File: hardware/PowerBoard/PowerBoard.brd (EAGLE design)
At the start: 90 x 56 mm, 136 parts, among them J1 CON-HRS-DM3AT, J2 CON-ZX62R-B-5P, J3 CON-FTSH-105-01-L-DV-K, J4 CON-S2B-PH-SM4-TB, J5 CON-PJ-102A, J6 CON-71741-0002-TOP, J7 SWITCH-CJS-1200-1200, M1 MOUNT-HOLE3.3, M2 MOUNT-HOLE3.3, M3 MOUNT-HOLE3.3, M4 MOUNT-HOLE3.3, M5 FIDUCIAL1X2, M6 FIDUCIAL1X2, M7 FIDUCIAL1X2, M8 FIDUCIAL1X2, Q1 SI2323CDS, Q2 SI2312CDS, Q3 SI2333CDS, Q4 SI2333CDS, SW1 SWITCH-SPST, SW2 SWITCH-MS12ASG30, SW3 SWITCH-ESWITCH-TL3340G, U1 LTC4361-2DC, U10 MAX9938FEUK, U11 MAX9938FEUK, U12 MAX9938FEUK, U13 STM32F10XCXT6, U14 LTC2942-1, U15 USBLC6-2, U2 LTC4085, U3 XC6220B331MR-G, U4 XC6220B331MR-G, U5 XC9236A15DMR-G, U6 MIC94043, U8 MAX9938FEUK, U9 MAX9938FEUK, X1 ECX-2236, X2 ECX-31B

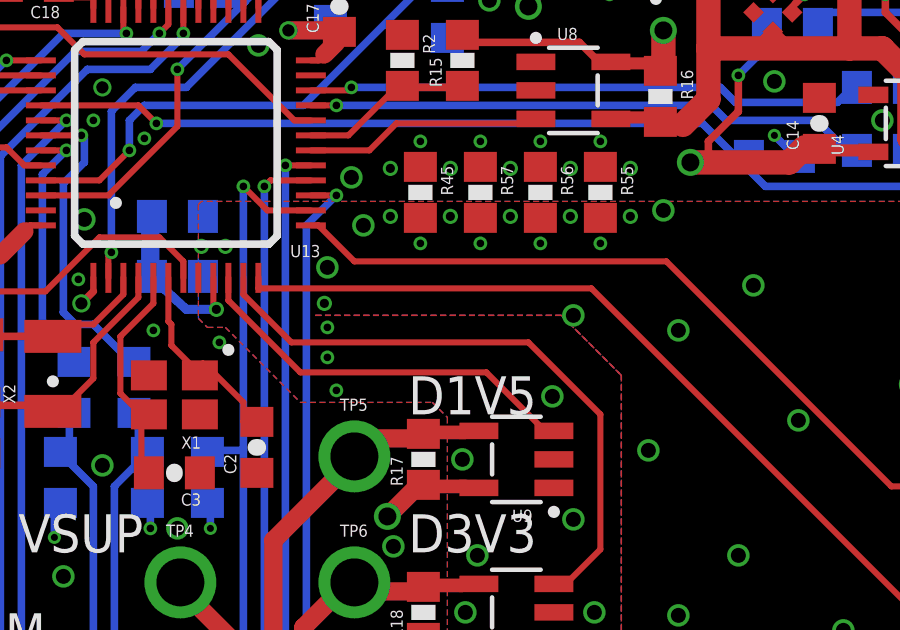
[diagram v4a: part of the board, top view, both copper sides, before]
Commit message: Modified ground plane cut-in.
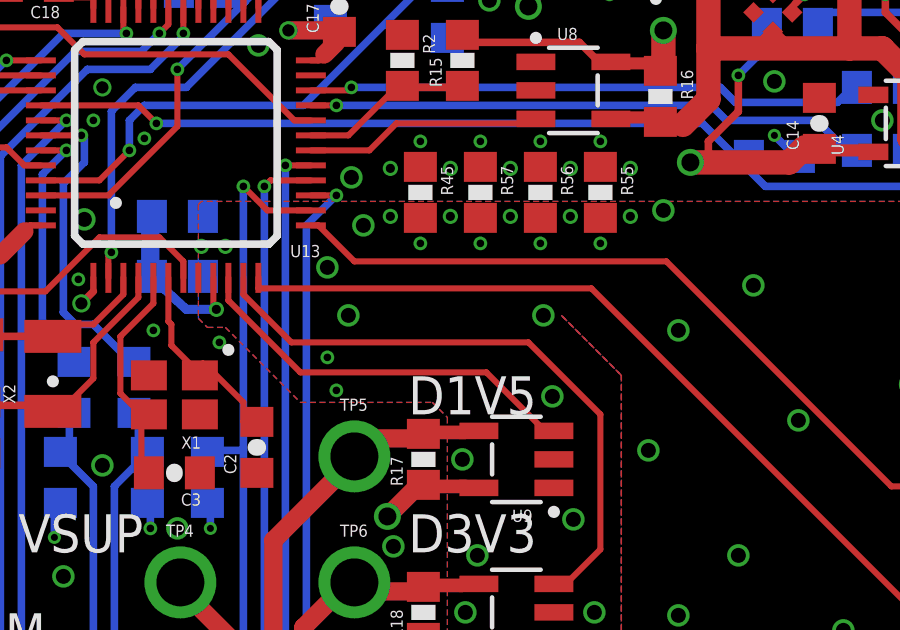
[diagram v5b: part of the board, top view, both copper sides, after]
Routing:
- net AGND: vias 87 -> 86
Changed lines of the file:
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@@
 <grid distance="0.5" unitdist="mm" unit="mm" style="lines" multiple="1" display="yes" altdistance="0.1" altunitdist="mm" altunit="mm"/>
 <layers>
-<layer number="1" name="Top" color="4" fill="1" visible="no" active="yes"/>
+<layer number="1" name="Top" color="4" fill="1" visible="yes" active="yes"/>
 <layer number="2" name="GND" color="2" fill="1" visible="no" active="yes"/>
 <layer number="3" name="SUPPLY" color="14" fill="1" visible="no" active="yes"/>
@@
 <layer number="15" name="Route15" color="4" fill="6" visible="no" active="no"/>
 <layer number="16" name="Bottom" color="11" fill="1" visible="no" active="yes"/>
-<layer number="17" name="Pads" color="2" fill="1" visible="no" active="yes"/>
-<layer number="18" name="Vias" color="2" fill="1" visible="no" active="yes"/>
+<layer number="17" name="Pads" color="2" fill="1" visible="yes" active="yes"/>
+<layer number="18" name="Vias" color="2" fill="1" visible="yes" active="yes"/>
 <layer number="19" name="Unrouted" color="6" fill="1" visible="yes" active="yes"/>
 <layer number="20" name="Dimension" color="15" fill="1" visible="yes" active="yes"/>
-<layer number="21" name="tPlace" color="7" fill="1" visible="no" active="yes"/>
+<layer number="21" name="tPlace" color="7" fill="1" visible="yes" active="yes"/>
 <layer number="22" name="bPlace" color="7" fill="1" visible="no" active="yes"/>
-<layer number="23" name="tOrigins" color="15" fill="1" visible="no" active="yes"/>
+<layer number="23" name="tOrigins" color="15" fill="1" visible="yes" active="yes"/>
 <layer number="24" name="bOrigins" color="15" fill="1" visible="no" active="yes"/>
 <layer number="25" name="tNames" color="7" fill="1" visible="no" active="yes"/>
@@
 <layer number="27" name="tValues" color="7" fill="1" visible="no" active="yes"/>
 <layer number="28" name="bValues" color="7" fill="1" visible="no" active="yes"/>
-<layer number="29" name="tStop" color="7" fill="3" visible="no" active="yes"/>
+<layer number="29" name="tStop" color="7" fill="3" visible="yes" active="yes"/>
 <layer number="30" name="bStop" color="7" fill="6" visible="no" active="yes"/>
 <layer number="31" name="tCream" color="7" fill="4" visible="no" active="yes"/>
@@
 <layer number="37" name="tTest" color="7" fill="1" visible="no" active="yes"/>
 <layer number="38" name="bTest" color="7" fill="1" visible="no" active="yes"/>
-<layer number="39" name="tKeepout" color="4" fill="11" visible="no" active="yes"/>
+<layer number="39" name="tKeepout" color="4" fill="11" visible="yes" active="yes"/>
 <layer number="40" name="bKeepout" color="1" fill="11" visible="no" active="yes"/>
 <layer number="41" name="tRestrict" color="4" fill="10" visible="no" active="yes"/>
@@
 <layer number="49" name="Reference" color="7" fill="1" visible="no" active="yes"/>
 <layer number="50" name="dxf" color="7" fill="1" visible="no" active="yes"/>
-<layer number="51" name="tDocu" color="14" fill="1" visible="no" active="yes"/>
+<layer number="51" name="tDocu" color="14" fill="1" visible="yes" active="yes"/>
 <layer number="52" name="bDocu" color="9" fill="1" visible="no" active="yes"/>
 <layer number="53" name="tGND_GNDA" color="7" fill="9" visible="no" active="no"/>
@@
 <via x="50.5" y="25" extent="1-16" drill="0.5"/>
 <via x="59.5" y="26" extent="1-16" drill="0.5"/>
-<via x="36.5" y="23" extent="1-16" drill="0.5"/>
+<via x="35.5" y="23" extent="1-16" drill="0.5"/>
 <via x="39" y="18.5" extent="1-16" drill="0.5"/>
 <via x="29.5" y="26" extent="1-16" drill="0.5"/>
@@
 <via x="42.5" y="24" extent="1-16" drill="0.5"/>
 <via x="28.3" y="24.6" extent="1-16" drill="0.5"/>
-<via x="28.2" y="23.4" extent="1-16" drill="0.3048"/>
 <via x="24.9" y="25.3" extent="1-16" drill="0.3048"/>
 <via x="24.1" y="25.3" extent="1-16" drill="0.3048"/>
@@
 <contactref element="U9" pad="1"/>
 <contactref element="U9" pad="2"/>
-<via x="28.3" y="22.6" extent="1-16" drill="0.254"/>
 <via x="28.3" y="21.6" extent="1-16" drill="0.254"/>
 <via x="28.6" y="20.5" extent="1-16" drill="0.254"/>
@@
 <via x="72.5" y="3.5" extent="1-16" drill="0.5"/>
 <via x="80" y="5" extent="1-16" drill="0.5"/>
+<via x="29" y="23" extent="1-16" drill="0.5"/>
 </signal>
 <signal name="VSUP">
@@
 <vertex x="38.1" y="21"/>
 <vertex x="36.1" y="23"/>
-<vertex x="27.9" y="23"/>
 <vertex x="36.1" y="23"/>
 <vertex x="38.1" y="21"/>
@@
 <vertex x="38.1" y="21"/>
 <vertex x="36.1" y="23"/>
-<vertex x="27.9" y="23"/>
 <vertex x="36.1" y="23"/>
 <vertex x="38.1" y="21"/>
@@
 <vertex x="38.1" y="21"/>
 <vertex x="36.1" y="23"/>
-<vertex x="27.9" y="23"/>
 <vertex x="36.1" y="23"/>
 <vertex x="38.1" y="21"/>
@@
 </signal>
 </signals>
-<errors>
-</errors>
 </board>
 </drawing>

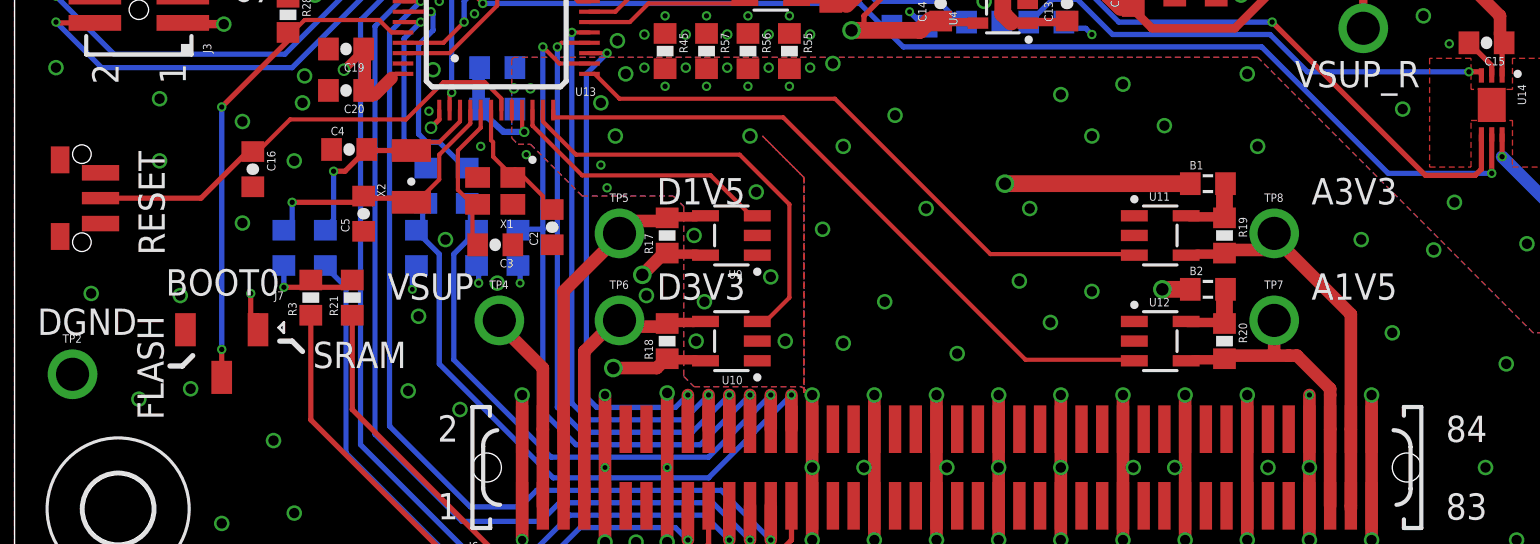
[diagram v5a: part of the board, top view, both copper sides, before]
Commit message: Adjusted BOOT switch and silk screen label positions.
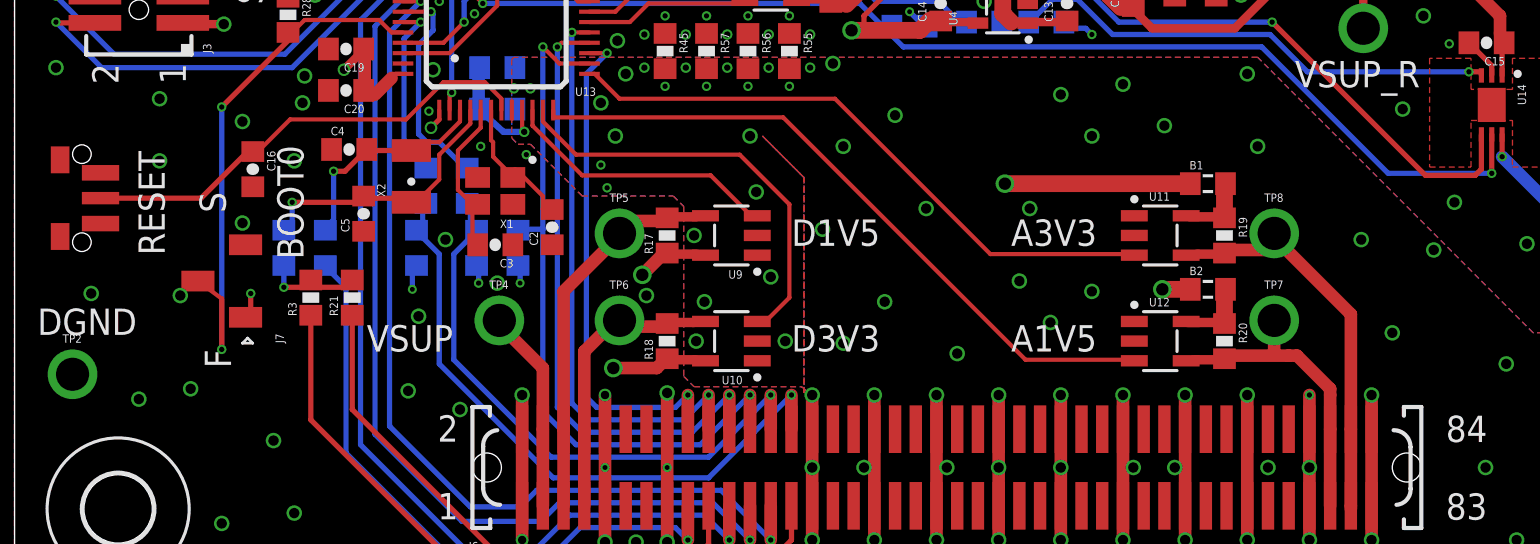
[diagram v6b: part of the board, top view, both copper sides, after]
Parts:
- moved J7 3.50 mm to (10.0, 16.0), turned to 90 degrees
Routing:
- net BOOT0: track 24.4 -> 26.9 mm
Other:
- board text added: "F"
- board text added: "S"
- board text removed: "FLASH"
- board text removed: "SRAM"
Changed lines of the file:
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@@
 <setting verticaltext="up"/>
 </settings>
-<grid distance="0.5" unitdist="mm" unit="mm" style="lines" multiple="1" display="yes" altdistance="0.1" altunitdist="mm" altunit="mm"/>
+<grid distance="1" unitdist="mm" unit="mm" style="lines" multiple="1" display="yes" altdistance="0.25" altunitdist="mm" altunit="mm"/>
 <layers>
 <layer number="1" name="Top" color="4" fill="1" visible="yes" active="yes"/>
@@
 <text x="60.75" y="54" size="1.27" layer="21" font="vector" rot="R180">OFF</text>
 <text x="80" y="54" size="1.27" layer="21" font="vector" rot="R180">ON</text>
-<text x="7.3" y="15.3" size="1.27" layer="21" font="vector">BOOT0</text>
+<text x="13.95" y="17.05" size="1.27" layer="21" font="vector" rot="R90">BOOT0</text>
 <text x="7.25" y="17.25" size="1.27" layer="21" font="vector" rot="R90">RESET</text>
 <text x="12" y="29.35" size="1.27" layer="21" font="vector" rot="R90">SWD</text>
@@
 <text x="85.25" y="37.25" size="1.27" layer="22" font="vector" rot="MR0">PWR SW</text>
 <text x="82.25" y="23.25" size="1.27" layer="22" font="vector" rot="MR0">BAT</text>
-<text x="14.4" y="11.8" size="1.27" layer="21" font="vector">SRAM</text>
-<text x="7.2" y="9.3" size="1.27" layer="21" font="vector" rot="R90">FLASH</text>
 <text x="82.15" y="13.4" size="1.27" layer="21" font="vector">AGND</text>
 <text x="1.1" y="13.4" size="1.27" layer="21" font="vector">DGND</text>
 <text x="67.25" y="35.75" size="1.27" layer="21" font="vector">VBAT</text>
-<text x="18" y="15.1" size="1.27" layer="21" font="vector">VSUP</text>
-<text x="31" y="15.1" size="1.27" layer="21" font="vector">D3V3</text>
-<text x="31" y="19.7" size="1.27" layer="21" font="vector">D1V5</text>
-<text x="62.6" y="15.1" size="1.27" layer="21" font="vector">A1V5</text>
-<text x="62.6" y="19.7" size="1.27" layer="21" font="vector">A3V3</text>
+<text x="17" y="12.6" size="1.27" layer="21" font="vector">VSUP</text>
+<text x="37.5" y="12.6" size="1.27" layer="21" font="vector">D3V3</text>
+<text x="37.5" y="17.7" size="1.27" layer="21" font="vector">D1V5</text>
+<text x="48.1" y="12.6" size="1.27" layer="21" font="vector">A1V5</text>
+<text x="48.1" y="17.7" size="1.27" layer="21" font="vector">A3V3</text>
 <text x="10.65" y="35.5" size="1.27" layer="21" font="vector">D3V3_STM</text>
 <text x="88" y="50" size="1.27" layer="21" font="vector" rot="R90">DGND</text>
@@
 <text x="70.75" y="2.75" size="1.27" layer="22" font="vector" rot="MR0">Vanderbilt University, ISIS</text>
 <circle x="54.5" y="5.2" radius="0.85" width="0.127" layer="22"/>
-<wire x1="13.9" y1="12.6" x2="13.4" y2="13.1" width="0.254" layer="21"/>
-<wire x1="13.4" y1="13.1" x2="12.8" y2="13.1" width="0.254" layer="21"/>
-<wire x1="8.6" y1="12.4" x2="8.1" y2="11.9" width="0.254" layer="21"/>
-<wire x1="8.1" y1="11.9" x2="7.5" y2="11.9" width="0.254" layer="21"/>
 <text x="11.9" y="44.65" size="1.27" layer="21" font="vector">VBUS</text>
+<text x="10.2" y="19.3" size="1.27" layer="21" font="vector" rot="R90">S</text>
+<text x="10.45" y="11.8" size="1.27" layer="21" font="vector" rot="R90">F</text>
 </plain>
 <attributes>
@@
 </element>
 <element name="SW3" library="powerboard" package="TL3340" value="SWITCH-ESWITCH-TL3340G" x="1.75" y="20" rot="R270"/>
-<element name="J7" library="powerboard" package="SWITCH-DIP-CJS" value="SWITCH-CJS-1200-1200" x="10" y="12.5" rot="R180"/>
+<element name="J7" library="powerboard" package="SWITCH-DIP-CJS" value="SWITCH-CJS-1200-1200" x="10" y="16" rot="R90"/>
 </elements>
 <signals>
@@
 <wire x1="8.1209" y1="28.4" x2="8.1209" y2="28.46" width="0.2032" layer="1"/>
 <wire x1="11.4" y1="14.35" x2="11.75" y2="14.35" width="0.2032" layer="1"/>
-<wire x1="11.75" y1="14.35" x2="11.75" y2="13.65" width="0.2032" layer="1"/>
+<wire x1="11.75" y1="14.35" x2="11.15" y2="14.25" width="0.2032" layer="1"/>
 <wire x1="16.9" y1="26.8" x2="16.85" y2="26.8" width="0.2032" layer="1"/>
 <wire x1="16.85" y1="26.8" x2="16.85" y2="27.2" width="0.2032" layer="1"/>
@@
 <wire x1="13.3" y1="27.7" x2="10" y2="24.4" width="0.254" layer="1"/>
 <wire x1="10" y1="24.4" x2="10" y2="12.7" width="0.254" layer="16"/>
-<wire x1="10" y1="12.7" x2="10" y2="11.9" width="0.254" layer="1"/>
+<wire x1="10" y1="12.7" x2="10" y2="15.15" width="0.254" layer="1"/>
 <contactref element="J7" pad="2"/>
 <via x="10" y="24.4" extent="1-16" drill="0.254"/>
@@
 <wire x1="13.2" y1="28" x2="13.2" y2="27.7" width="0.2032" layer="1"/>
 <wire x1="13.2" y1="27.7" x2="13.3" y2="27.7" width="0.2032" layer="1"/>
-<wire x1="10" y1="11.9" x2="10" y2="11.35" width="0.2032" layer="1"/>
+<wire x1="10" y1="15.15" x2="8.85" y2="16" width="0.2032" layer="1"/>
 </signal>
 <signal name="N$29">

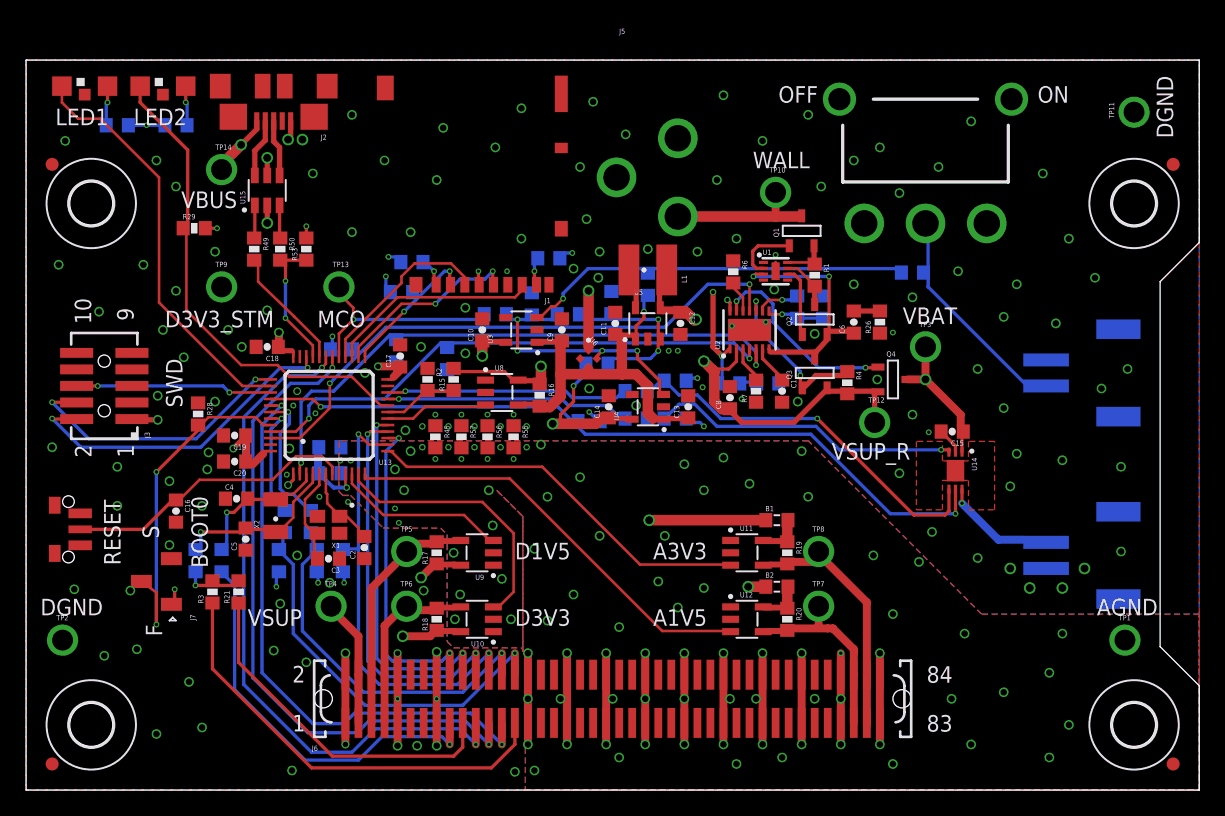
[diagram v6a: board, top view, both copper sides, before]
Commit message: - Logos on silk screen - Board name updated
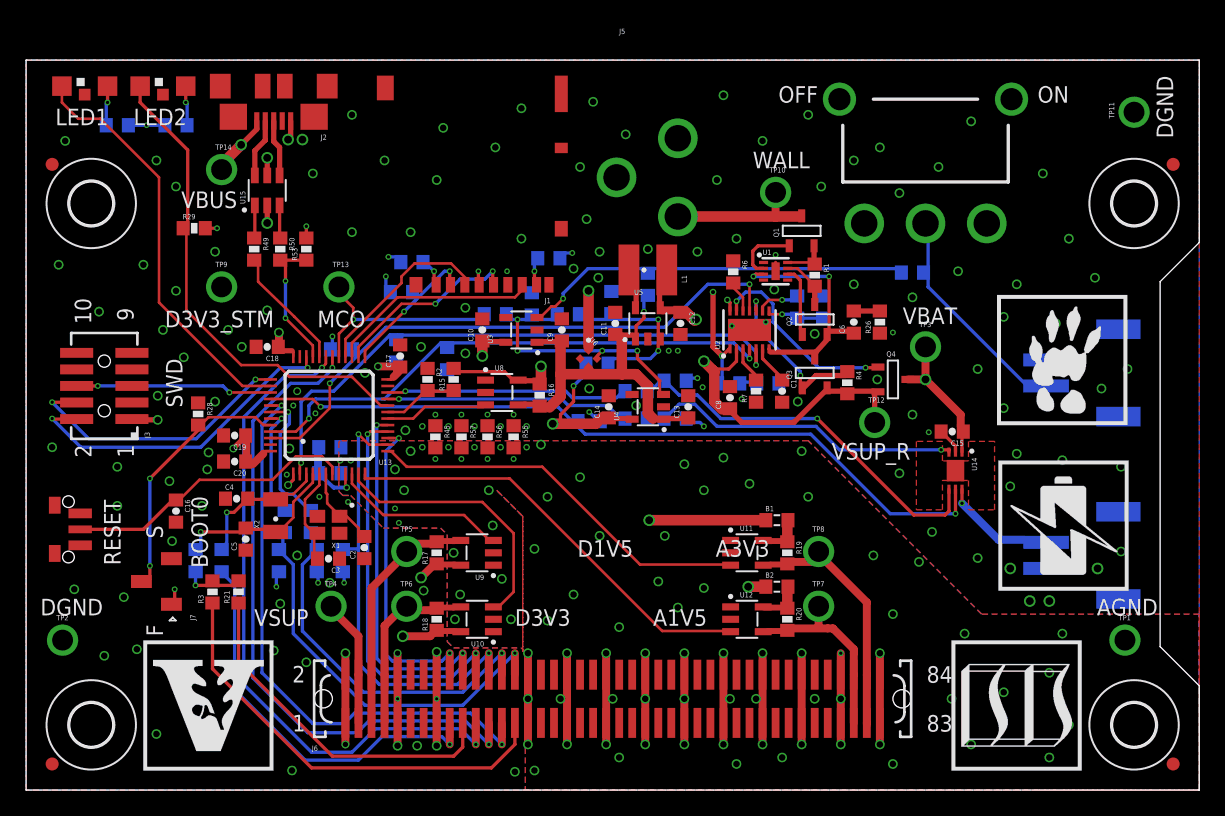
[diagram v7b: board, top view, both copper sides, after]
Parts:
- removed LOGO7: LOGO-MARMOTE-600MIL-10MM-AU, Logo:LOGO-MARMOTE-10MM-GOLD
- added LOGO2: LOGO-BATTERY-600MIL-10MM-SS, Logo:LOGO-BATTERY-10MM-SILKSCREEN
- LOGO1: value LOGO-BATTERY-600MIL-10MM-AU -> LOGO-ISIS-600MIL-10MM-SS; device Logo:LOGO-BATTERY-10MM-GOLD -> Logo:LOGO-ISIS-10MM-SILKSCREEN
- LOGO5: value LOGO-VANDERBILT-600MIL-10MM-AU -> LOGO-VANDERBILT-600MIL-10MM-SS; device Logo:LOGO-VANDERBILT-10MM-GOLD -> Logo:LOGO-VANDERBILT-10MM-SILKSCREEN
- LOGO6: value LOGO-ISIS-600MIL-10MM-AU -> LOGO-MARMOTE-600MIL-10MM-SS; device Logo:LOGO-ISIS-10MM-GOLD -> Logo:LOGO-MARMOTE-10MM-SILKSCREEN
- moved LOGO6 25.9 mm to (74.5, 28.0)
- moved LOGO1 14.2 mm to (71.0, 1.50)
- moved LOGO5 2.00 mm to (9.00, 1.50)
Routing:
- net BOOT0: track 26.9 -> 20.5 mm
